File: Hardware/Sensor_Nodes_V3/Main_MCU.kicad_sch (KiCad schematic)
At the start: 21 parts, among them J6 Conn_01x27_Socket, J7 Conn_01x27_Socket, U1 STM32G474RBTx, U3 MCP2542FDxMF, U6 MCP2542FDxMF

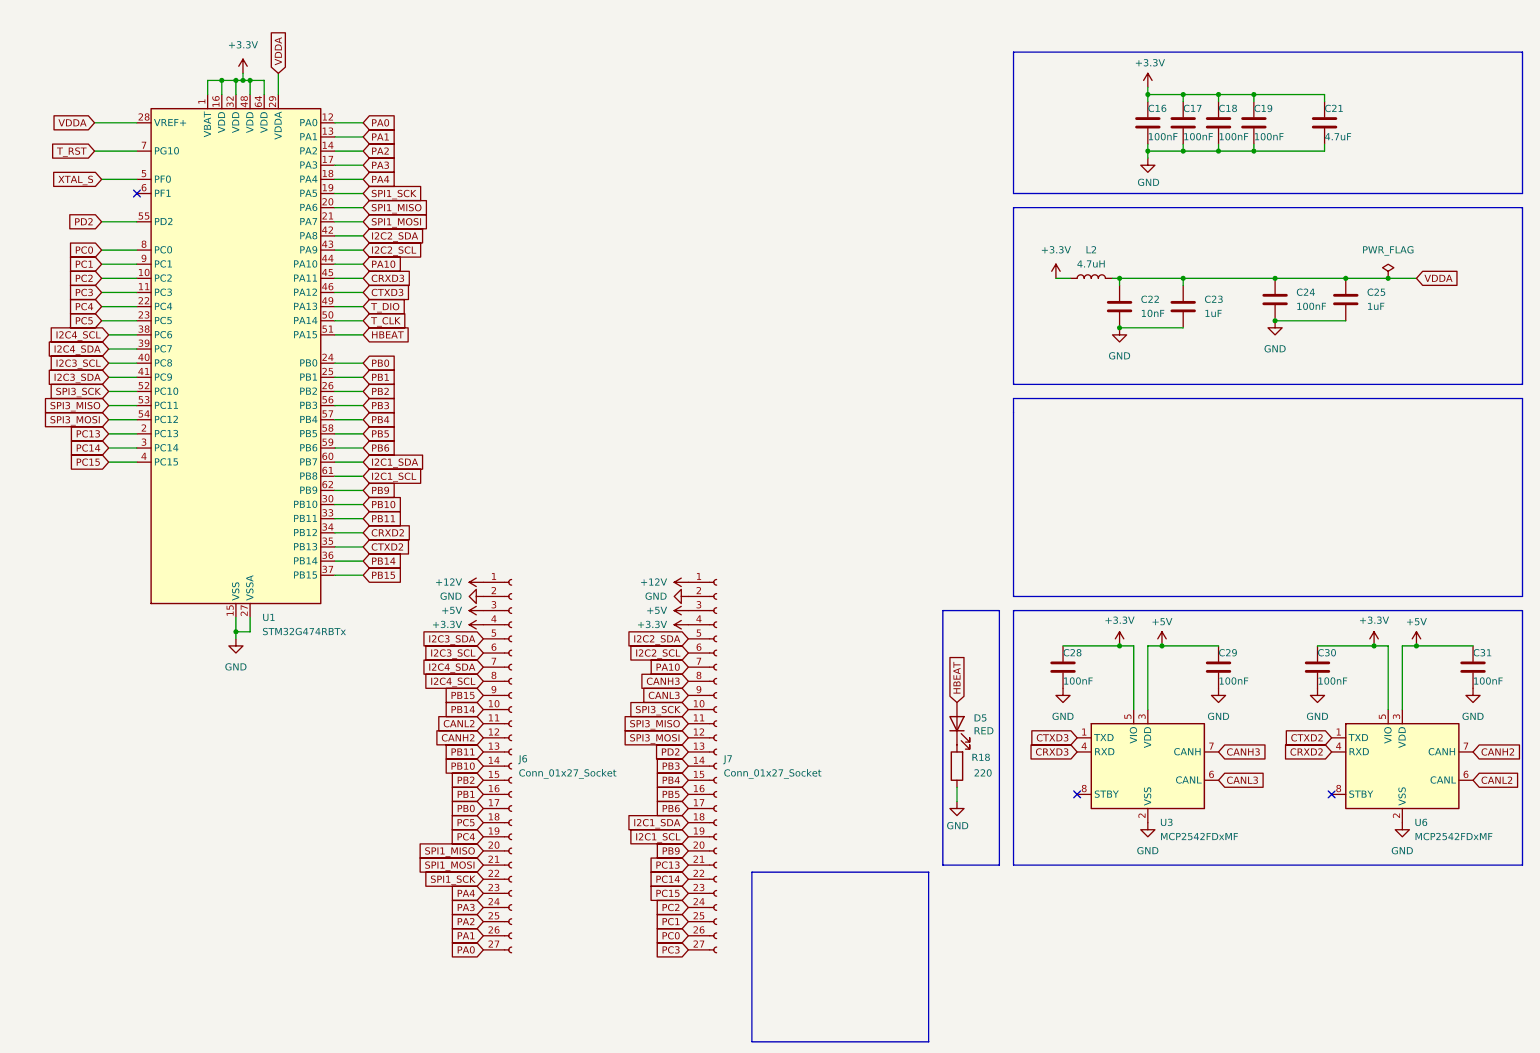
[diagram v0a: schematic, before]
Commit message: alt placement made
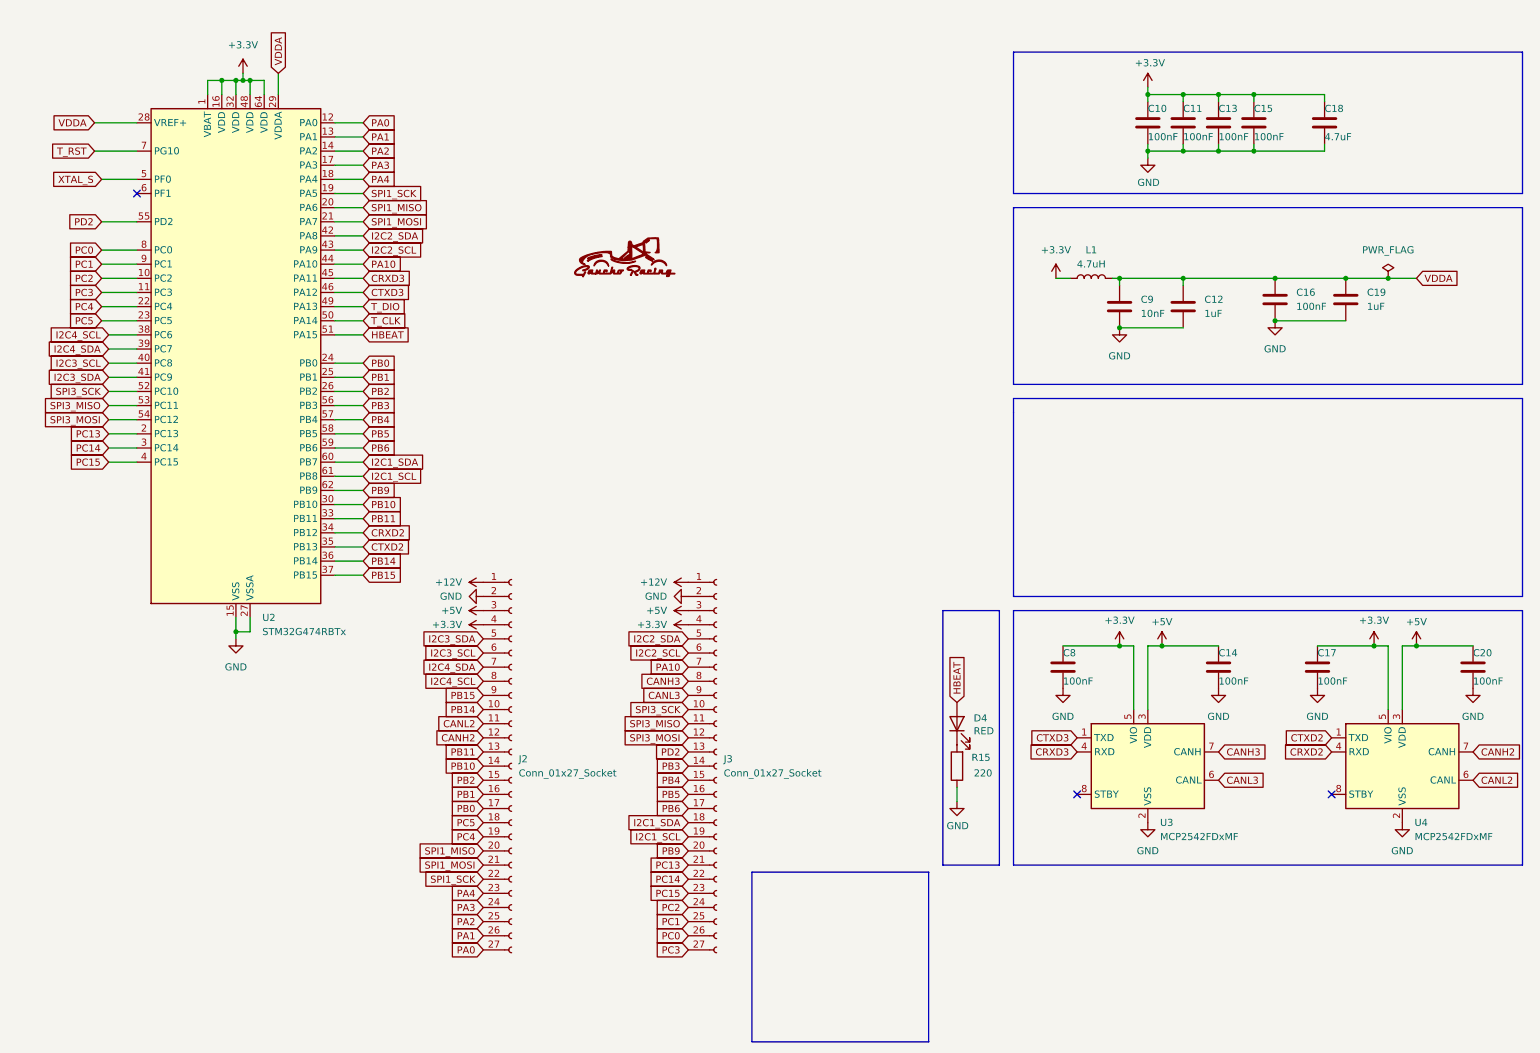
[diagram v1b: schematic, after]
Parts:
- renumbered C16 to C10, C17 to C11, C23 to C12, C18 to C13, C29 to C14, C19 to C15, C24 to C16, C30 to C17, C21 to C18, C25 to C19, C31 to C20, C28 to C8, C22 to C9, D5 to D4, J6 to J2, J7 to J3, L2 to L1, R18 to R15, U1 to U2, U6 to U4

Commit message: rerouted a little and added swo
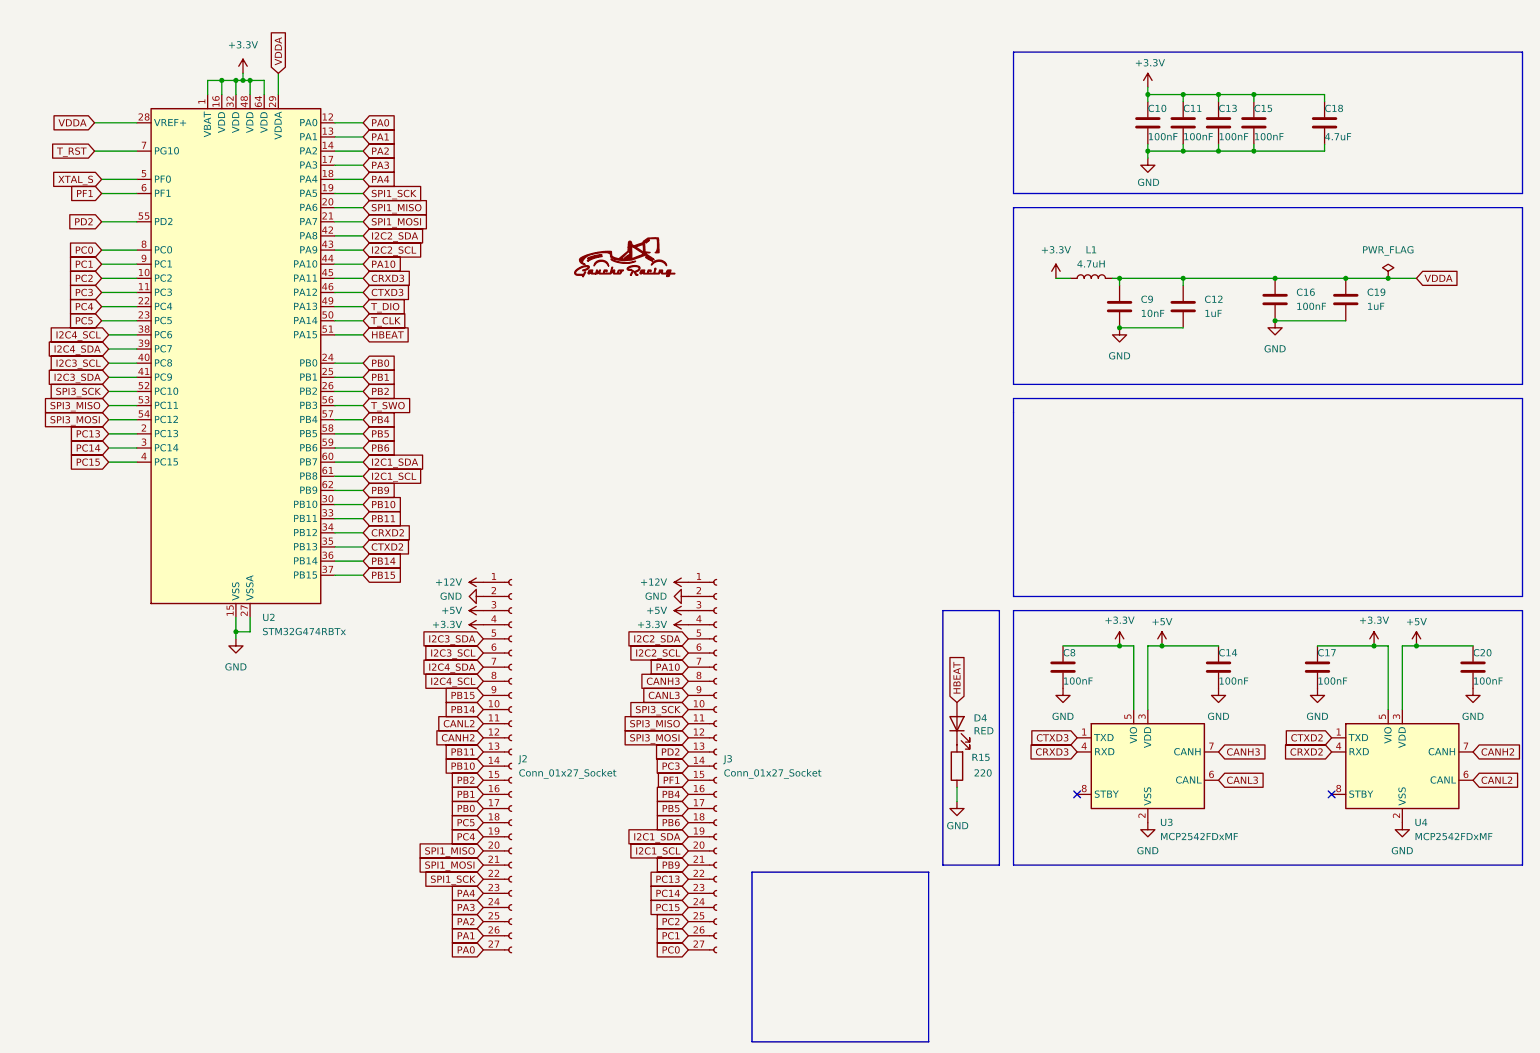
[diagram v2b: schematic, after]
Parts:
- C9: LCSC C19666 -> C57112
- L1: LCSC C1034 -> C1049
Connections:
- net I2C1_SCL: now also J3.20 (Pin_20); no longer J3.19 (Pin_19)
- net I2C1_SDA: now also J3.19 (Pin_19); no longer J3.18 (Pin_18)
- net PB4: now also J3.16 (Pin_16); no longer J3.15 (Pin_15)
- net PB5: now also J3.17 (Pin_17); no longer J3.16 (Pin_16)
- net PB6: now also J3.18 (Pin_18); no longer J3.17 (Pin_17)
- net PB9: now also J3.21 (Pin_21); no longer J3.20 (Pin_20)
- net PC0: now also J3.27 (Pin_27); no longer J3.26 (Pin_26)
- net PC1: now also J3.26 (Pin_26); no longer J3.25 (Pin_25)
- net PC13: now also J3.22 (Pin_22); no longer J3.21 (Pin_21)
- net PC14: now also J3.23 (Pin_23); no longer J3.22 (Pin_22)
- net PC15: now also J3.24 (Pin_24); no longer J3.23 (Pin_23)
- net PC2: now also J3.25 (Pin_25); no longer J3.24 (Pin_24)
- net PC3: now also J3.14 (Pin_14); no longer J3.27 (Pin_27)
- net PF1: now reaches U2.6 (PF1)
- net PF1: now also J3.15 (Pin_15)
- net PB3 renamed T_SWO
- net T_SWO: no longer J3.14 (Pin_14)
- no-connect marks 3 -> 2

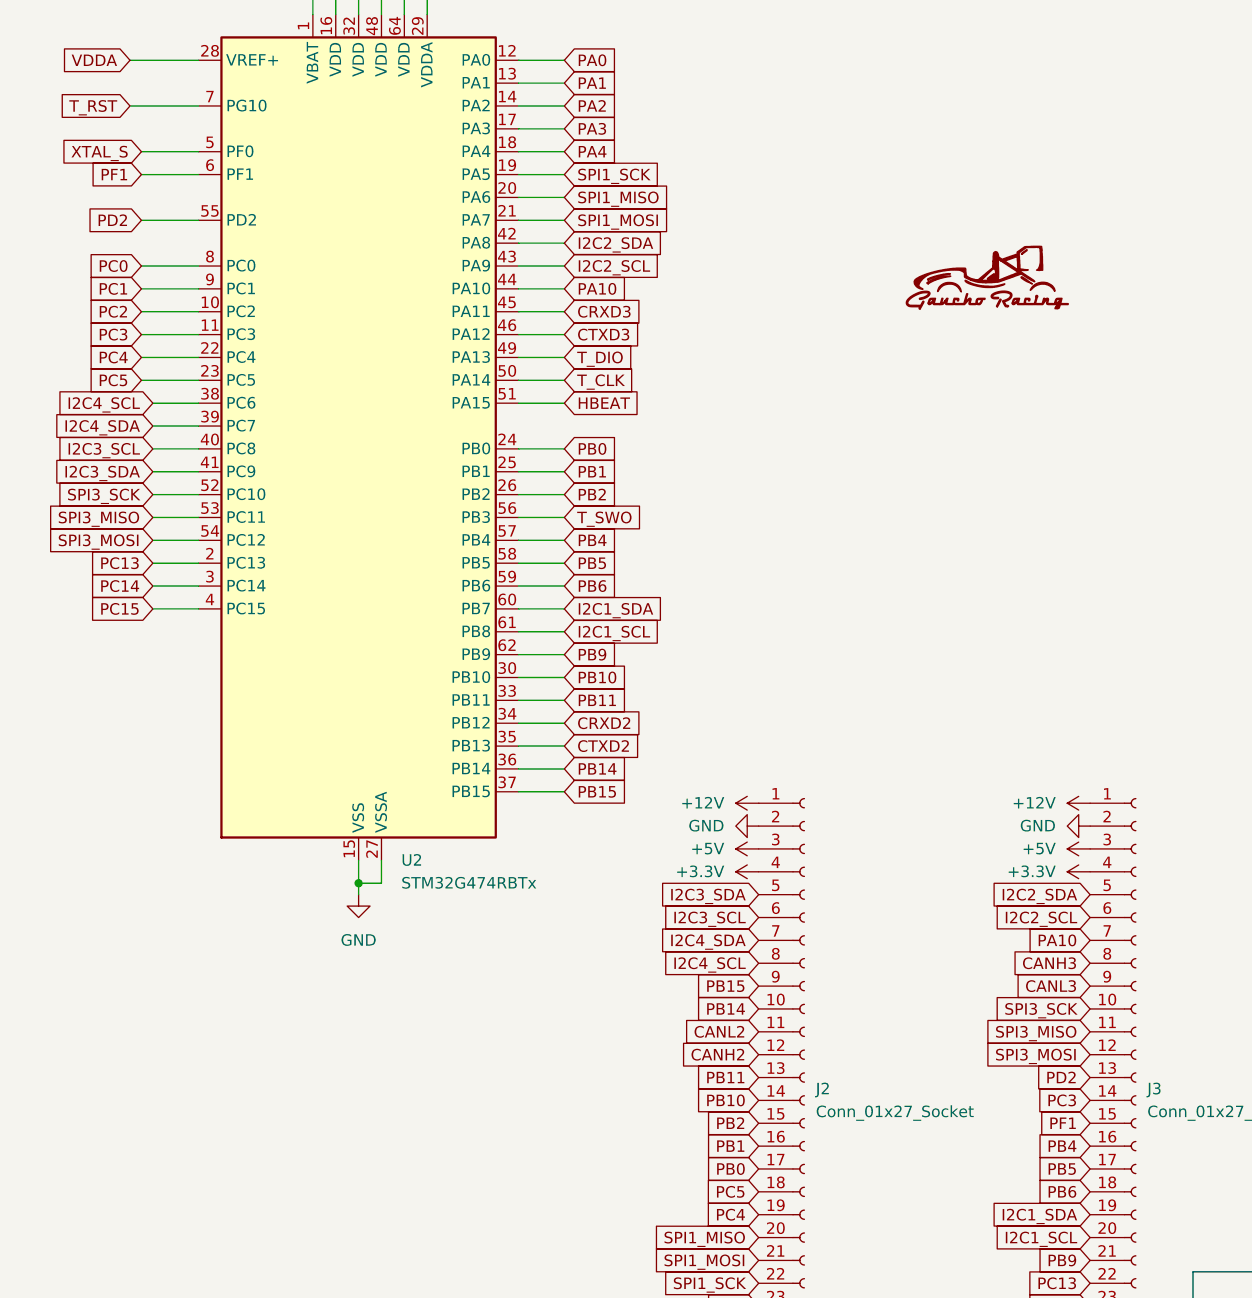
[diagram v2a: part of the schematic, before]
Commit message: some alt placement finished, moved xtal. will branch and rotate stlink by 90
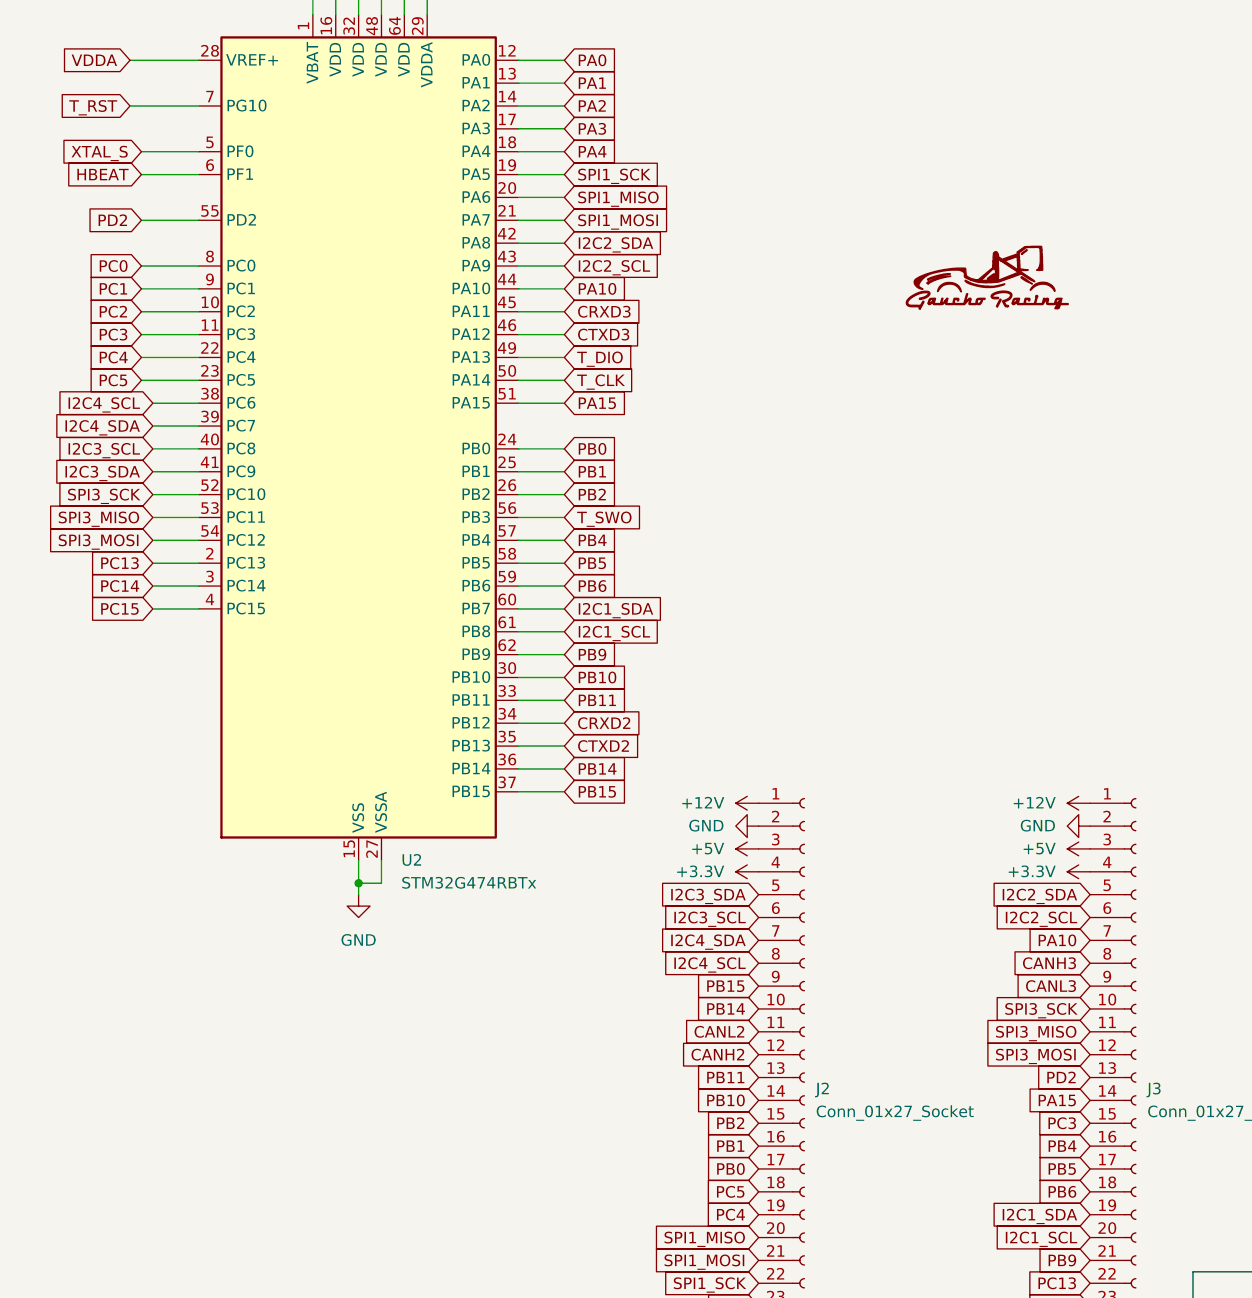
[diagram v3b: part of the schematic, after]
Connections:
- net HBEAT: now also U2.6 (PF1); no longer U2.51 (PA15)
- net PC3: now also J3.15 (Pin_15); no longer J3.14 (Pin_14)
- removed net PF1: J3.15 (Pin_15), U2.6 (PF1)
- new net PA15: J3.14 (Pin_14), U2.51 (PA15)
